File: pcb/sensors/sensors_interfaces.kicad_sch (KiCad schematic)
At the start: 23 parts, among them J3 CAN BUS, J4 DIMMER I2C, J5 DIMMER I2C, J6 FLOW HALL, J7 VALVE SSR, J8 BOILER SSR, Q2 AO3401A, Q3 2N7002, U4 TJA1051T/3, U5 TMP102AIDRLR

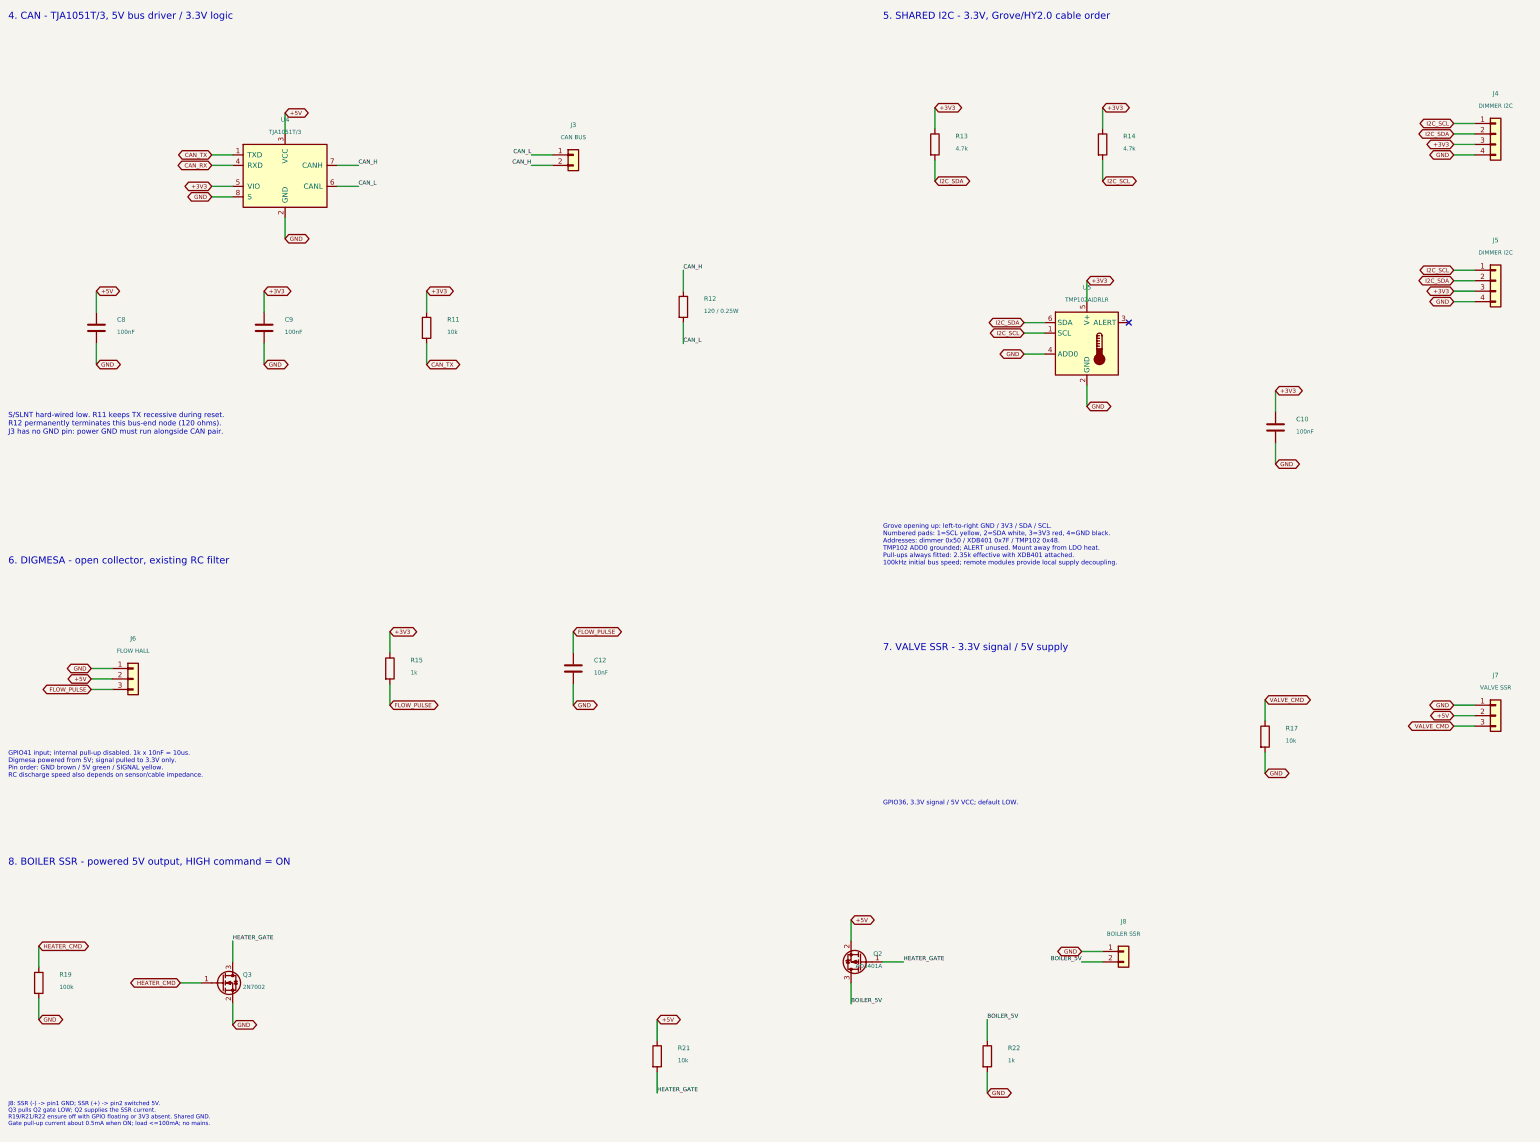
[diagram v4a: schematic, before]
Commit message: Replace sensors MINI controller with socketed XIAO ESP32-S3
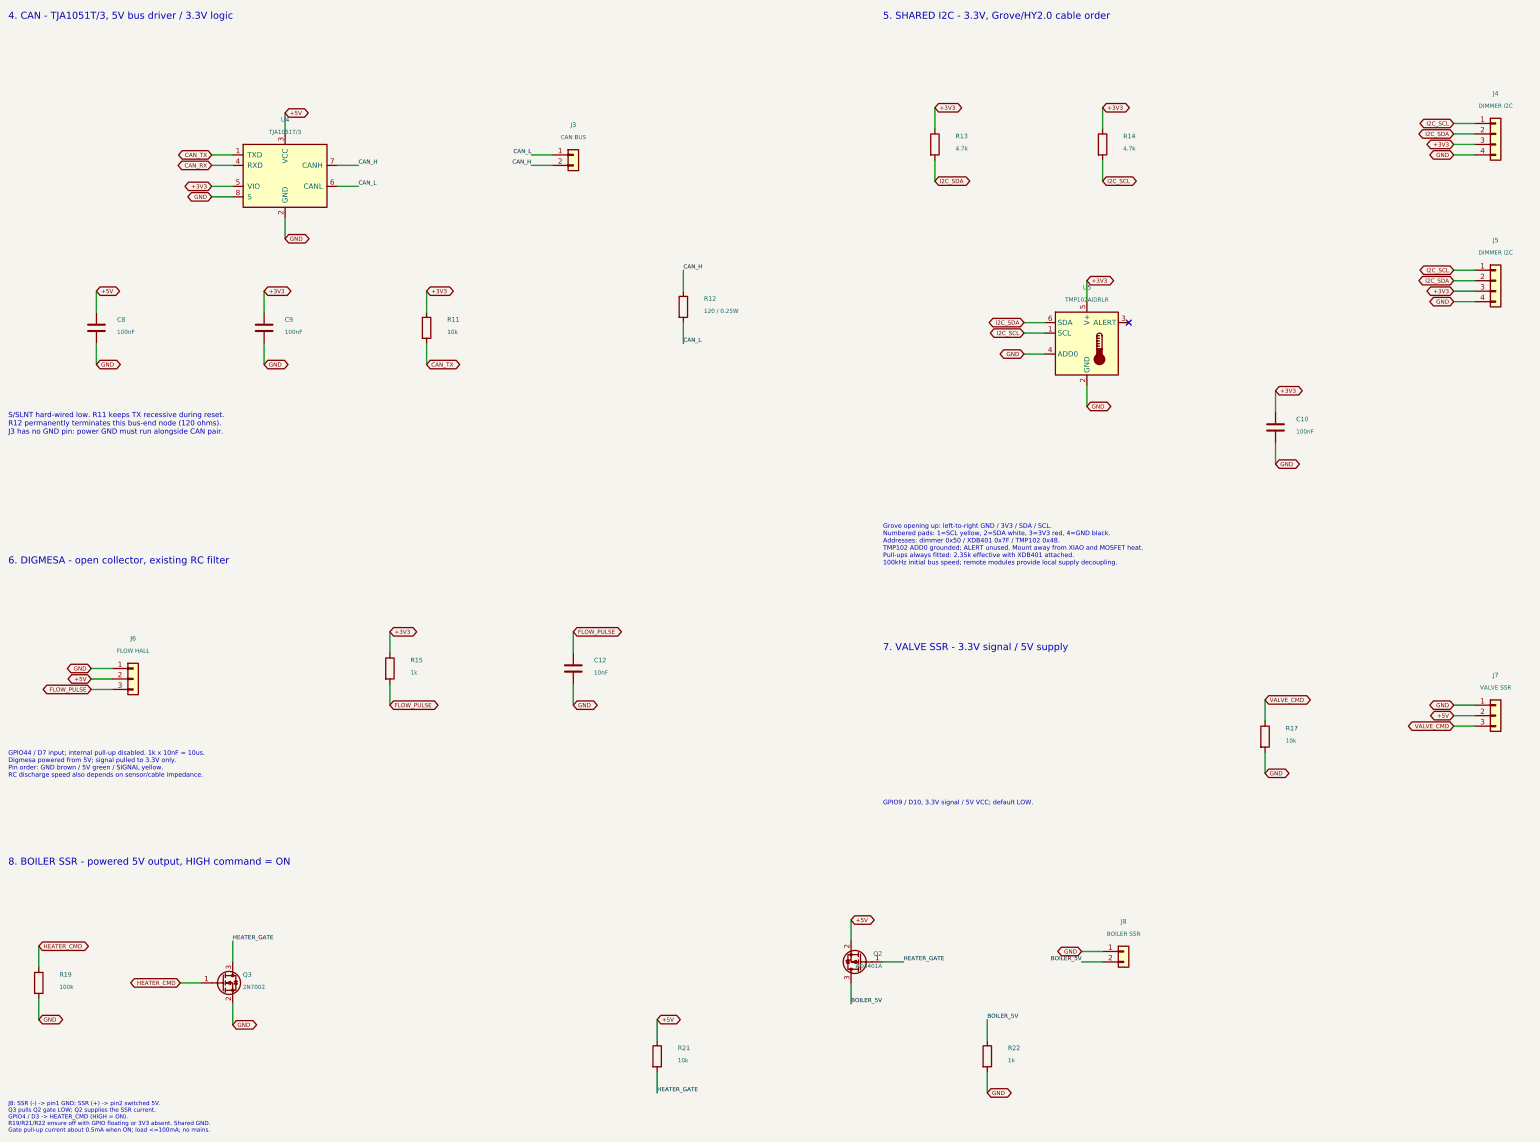
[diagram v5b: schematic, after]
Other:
- note added: "GPIO44 / D7 input; internal pull-up disabled. 1k x 10nF = 10us. Digmesa powered from 5V; signal pulled to 3.3V only. Pin order: GND brown / 5V green / SIGNAL yellow. RC discharge speed also depends on sensor/cable impedance."
- note added: "GPIO9 / D10, 3.3V signal / 5V VCC; default LOW."
- note added: "Grove opening up: left-to-right GND / 3V3 / SDA / SCL. Numbered pads: 1=SCL yellow, 2=SDA white, 3=3V3 red, 4=GND black. Addresses: dimmer 0x50 / XDB401 0x7F / TMP102 0x48. TMP102 ADD0 grounded; ALERT unused. Mount away from XIAO and MOSFET heat. Pull-ups always fitted: 2.35k effective with XDB401 attached. 100kHz initial bus speed; remote modules provide local supply decoupling."
- note added: "J8: SSR (-) -> pin1 GND; SSR (+) -> pin2 switched 5V. Q3 pulls Q2 gate LOW; Q2 supplies the SSR current. GPIO4 / D3 -> HEATER_CMD (HIGH = ON). R19/R21/R22 ensure off with GPIO floating or 3V3 absent. Shared GND. Gate pull-up current about 0.5mA when ON; load <=100mA; no mains."
- note removed: "GPIO36, 3.3V signal / 5V VCC; default LOW."
- note removed: "GPIO41 input; internal pull-up disabled. 1k x 10nF = 10us. Digmesa powered from 5V; signal pulled to 3.3V only. Pin order: GND brown / 5V green / SIGNAL yellow. RC discharge speed also depends on sensor/cable impedance."
- note removed: "Grove opening up: left-to-right GND / 3V3 / SDA / SCL. Numbered pads: 1=SCL yellow, 2=SDA white, 3=3V3 red, 4=GND black. Addresses: dimmer 0x50 / XDB401 0x7F / TMP102 0x48. TMP102 ADD0 grounded; ALERT unused. Mount away from LDO heat. Pull-ups always fitted: 2.35k effective with XDB401 attached. 100kHz initial bus speed; remote modules provide local supply decoupling."
- note removed: "J8: SSR (-) -> pin1 GND; SSR (+) -> pin2 switched 5V. Q3 pulls Q2 gate LOW; Q2 supplies the SSR current. R19/R21/R22 ensure off with GPIO floating or 3V3 absent. Shared GND. Gate pull-up current about 0.5mA when ON; load <=100mA; no mains."
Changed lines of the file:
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@@
 		(rev "A")
 		(company "CoffeeFlow")
-		(comment 1 "CAN-only / USB flash power OR external 5V")
+		(comment 1 "XIAO sockets - schematic only; PCB pending")
 	)
 	(text "8. BOILER SSR - powered 5V output, HIGH command = ON"
@@
 		)
 	)
-	(text "Grove opening up: left-to-right GND / 3V3 / SDA / SCL.\nNumbered pads: 1=SCL yellow, 2=SDA white, 3=3V3 red, 4=GND black.\nAddresses: dimmer 0x50 / XDB401 0x7F / TMP102 0x48.\nTMP102 ADD0 grounded; ALERT unused. Mount away from LDO heat.\nPull-ups always fitted: 2.35k effective with XDB401 attached.\n100kHz initial bus speed; remote modules provide local supply decoupling."
+	(text "Grove opening up: left-to-right GND / 3V3 / SDA / SCL.\nNumbered pads: 1=SCL yellow, 2=SDA white, 3=3V3 red, 4=GND black.\nAddresses: dimmer 0x50 / XDB401 0x7F / TMP102 0x48.\nTMP102 ADD0 grounded; ALERT unused. Mount away from XIAO and MOSFET heat.\nPull-ups always fitted: 2.35k effective with XDB401 attached.\n100kHz initial bus speed; remote modules provide local supply decoupling."
 		(exclude_from_sim no)
 		(at 230 139 0)
@@
 		)
 	)
-	(text "GPIO36, 3.3V signal / 5V VCC; default LOW."
+	(text "GPIO9 / D10, 3.3V signal / 5V VCC; default LOW."
 		(exclude_from_sim no)
 		(at 230 206 0)
@@
 		)
 	)
-	(text "J8: SSR (-) -> pin1 GND; SSR (+) -> pin2 switched 5V.\nQ3 pulls Q2 gate LOW; Q2 supplies the SSR current.\nR19/R21/R22 ensure off with GPIO floating or 3V3 absent. Shared GND.\nGate pull-up current about 0.5mA when ON; load <=100mA; no mains."
+	(text "J8: SSR (-) -> pin1 GND; SSR (+) -> pin2 switched 5V.\nQ3 pulls Q2 gate LOW; Q2 supplies the SSR current.\nGPIO4 / D3 -> HEATER_CMD (HIGH = ON).\nR19/R21/R22 ensure off with GPIO floating or 3V3 absent. Shared GND.\nGate pull-up current about 0.5mA when ON; load <=100mA; no mains."
 		(exclude_from_sim no)
 		(at 18 279 0)
@@
 		)
 	)
-	(text "GPIO41 input; internal pull-up disabled. 1k x 10nF = 10us.\nDigmesa powered from 5V; signal pulled to 3.3V only.\nPin order: GND brown / 5V green / SIGNAL yellow.\nRC discharge speed also depends on sensor/cable impedance."
+	(text "GPIO44 / D7 input; internal pull-up disabled. 1k x 10nF = 10us.\nDigmesa powered from 5V; signal pulled to 3.3V only.\nPin order: GND brown / 5V green / SIGNAL yellow.\nRC discharge speed also depends on sensor/cable impedance."
 		(exclude_from_sim no)
 		(at 18 194 0)
